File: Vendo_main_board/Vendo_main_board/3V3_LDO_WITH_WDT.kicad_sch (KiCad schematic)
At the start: 16 parts, among them U2 74AHCT1G125, U2 TPL5010, U4 TPS73733DCQR

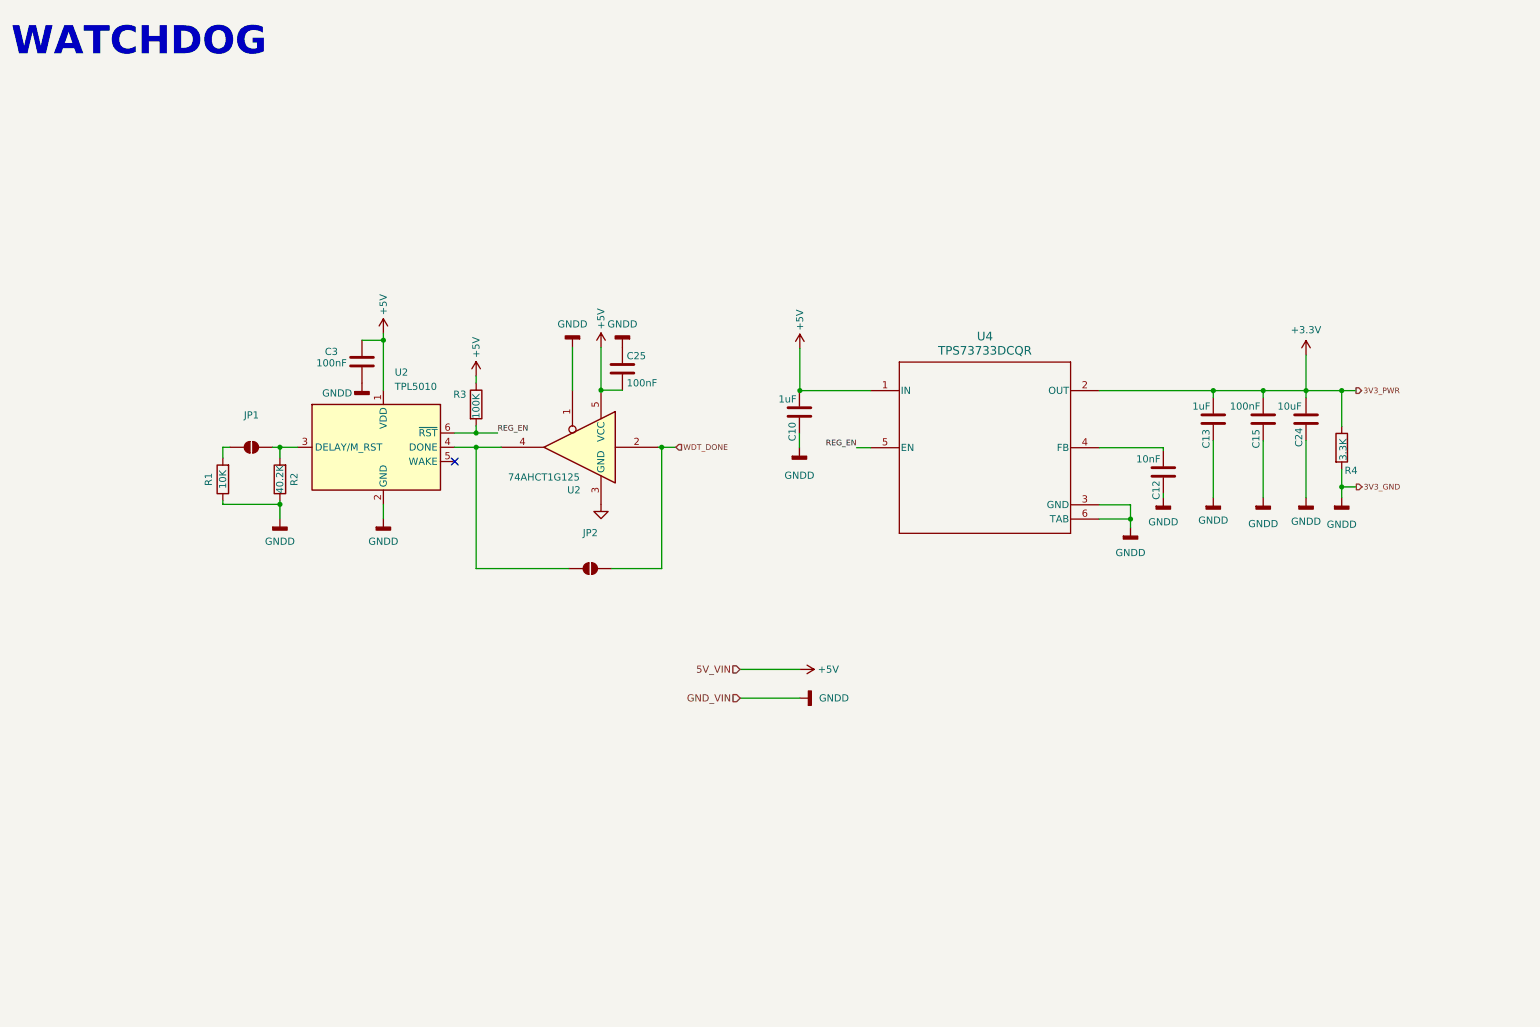
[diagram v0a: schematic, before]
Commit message: -update schematic
-recheck lcsc part number ,value
-check and update footprint assignment
-add load switch for the wdt and ldo combination

-add link for quick connect footprint must be discuss for clarification
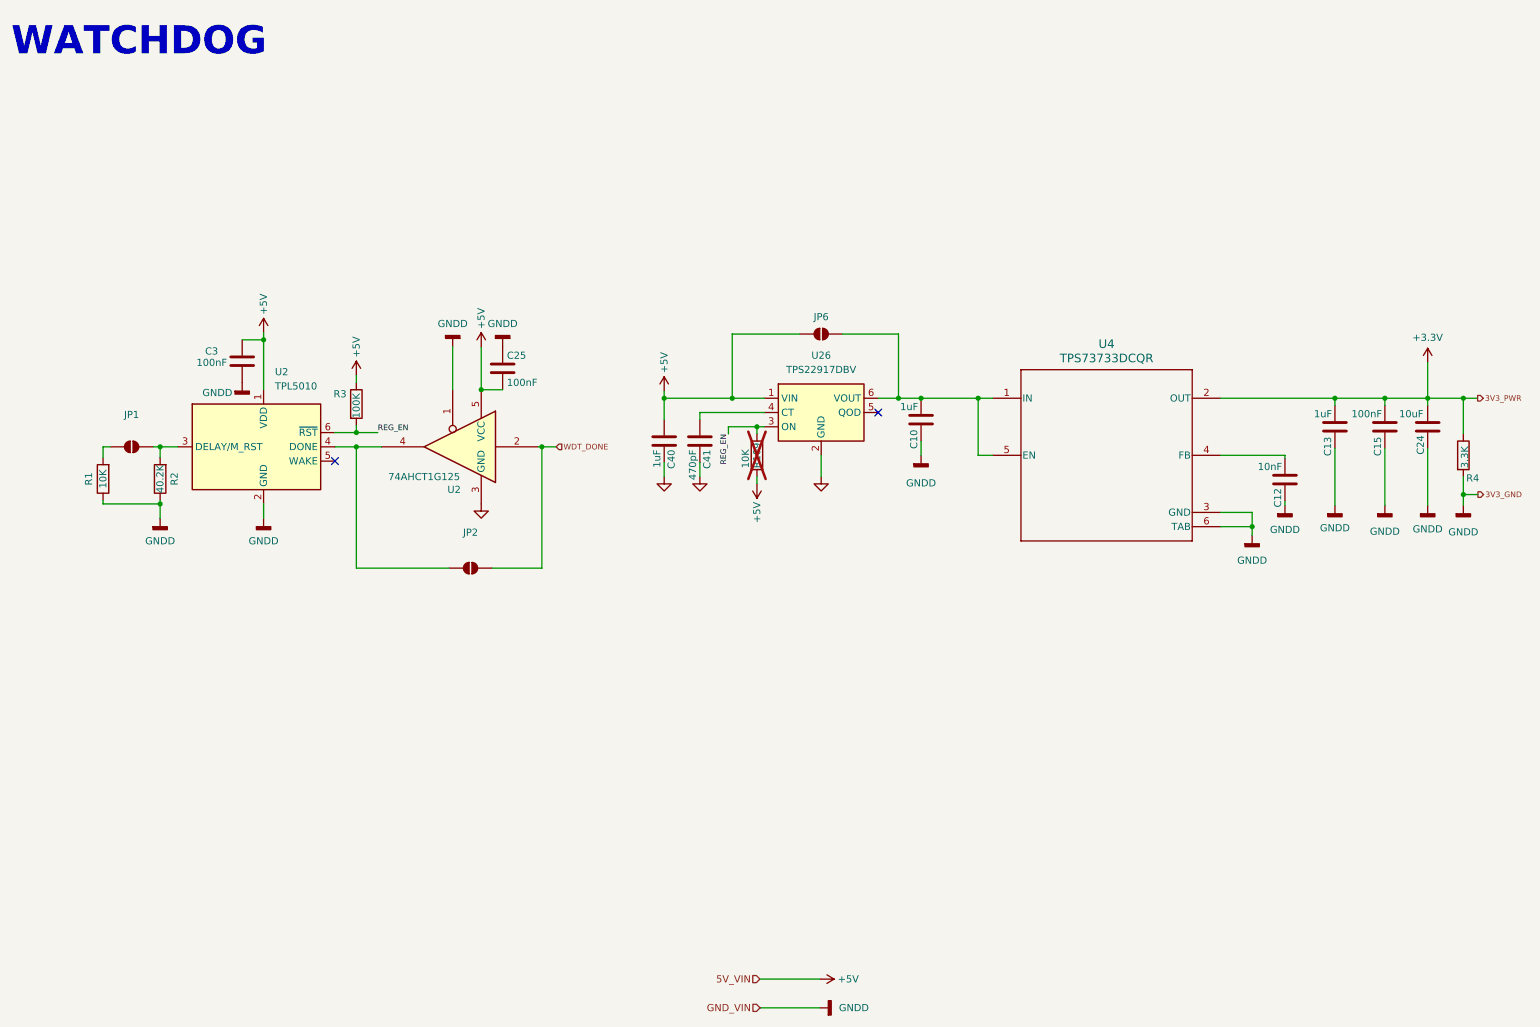
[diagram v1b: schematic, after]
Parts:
- added C40: 1uF, Capacitor_SMD:C_0805_2012Metric_Pad1.18x1.45mm_HandSolder, symbol Device:C
- added C41: 470pF, Capacitor_SMD:C_0603_1608Metric_Pad1.08x0.95mm_HandSolder, symbol Device:C
- added JP6: SolderJumper_2_Open, Jumper:SolderJumper-2_P1.3mm_Open_Pad1.0x1.5mm, symbol Jumper:SolderJumper_2_Open
- added R109: 10K, Resistor_SMD:R_0603_1608Metric_Pad0.98x0.95mm_HandSolder, symbol Device:R
- added U26: TPS22917DBV, Package_TO_SOT_SMD:SOT-23-6, symbol Power_Management:TPS22917DBV
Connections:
- net +5V: now also C40.2, JP6.1 (A), R109.2, U26.1 (VIN); no longer C10.2, U4.1 (IN)
- net GND: now also C40.1, C41.1, U26.2 (GND)
- net REG_EN: now also R109.1, U26.3 (ON); no longer U4.5 (EN)
- new net: C41.2, U26.4 (CT)
- new net: C10.2, JP6.2 (B), U26.6 (VOUT), U4.1 (IN), U4.5 (EN)
- no-connect marks 1 -> 2
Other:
- moved on the sheet: C10, C12, C13, C15, C24, C25, C3, JP1, JP2, R1, R2, R3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

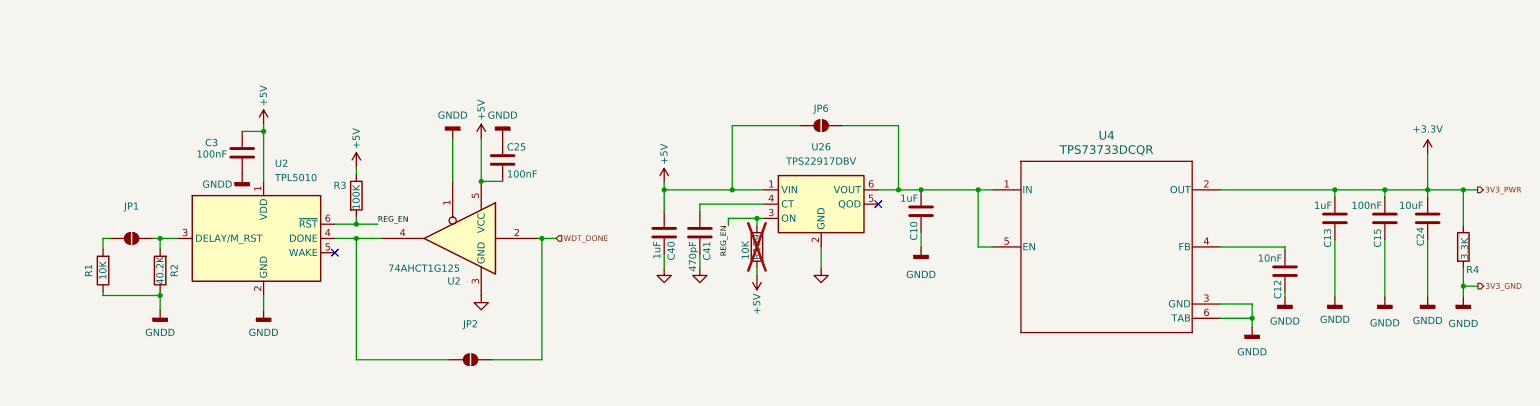
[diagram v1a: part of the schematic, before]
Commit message: -update scheme and pcb placement
update scheme and footprint
added spade connectors
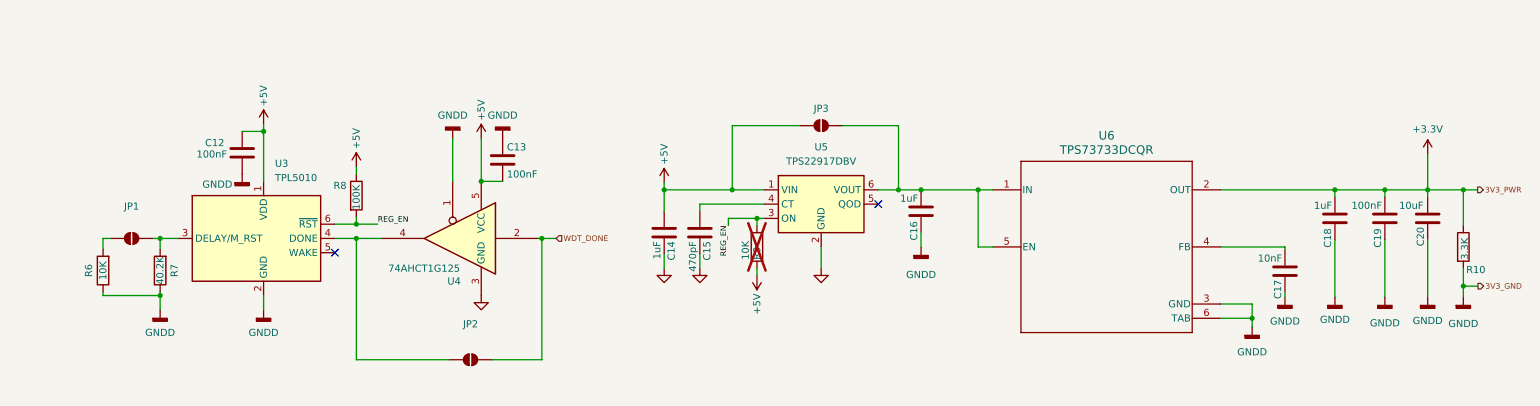
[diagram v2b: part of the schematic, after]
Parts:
- renumbered C3 to C12, C25 to C13, C40 to C14, C41 to C15, C10 to C16, C12 to C17, C13 to C18, C15 to C19, C24 to C20, JP6 to JP3, R4 to R10, R1 to R6, R2 to R7, R3 to R8, R109 to R9, U2 to U3, U2 to U4, U26 to U5, U4 to U6
